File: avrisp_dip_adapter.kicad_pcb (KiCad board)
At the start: 2 copper layers, 12.7 x 16.5 mm, 2 parts, among them J1 Conn_01x06, J2 AVR-ISP-6

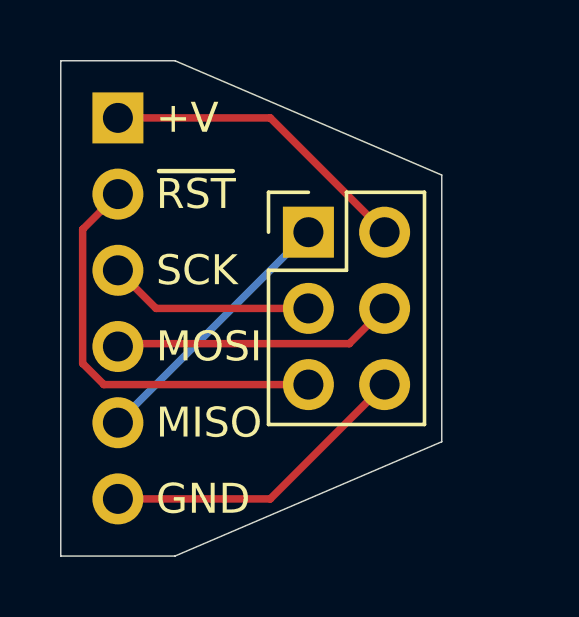
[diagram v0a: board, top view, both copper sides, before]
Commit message: Add a little more separation
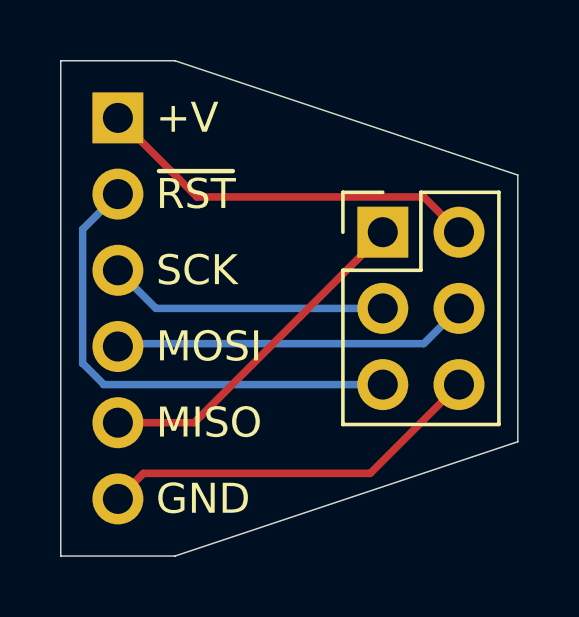
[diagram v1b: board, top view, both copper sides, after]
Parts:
- added REF**: Logo_WM, Symbol:Logo_WM, B.Cu at (158.0, 90.1)
- moved J2 2.48 mm to (162.5, 91.4)
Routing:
- net MOSI: track 9.42 -> 12.0 mm
- net MISO: track 8.98 -> 11.5 mm
- net SCK: track 6.88 -> 9.36 mm
- net ~RST~: track 13.9 -> 16.4 mm
- net V+: track 10.5 -> 12.9 mm
- net GND: track 10.5 -> 12.9 mm
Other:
- board size 12.7 x 16.5 mm -> 15.2 x 16.5 mm
- board text added: "v0.0.0 12/18/20"
